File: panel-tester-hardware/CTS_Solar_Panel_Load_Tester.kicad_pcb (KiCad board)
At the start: 2 copper layers, 57 x 67.5 mm, 18 parts, among them J1 Screw_Terminal_01x02, J2 Conn_01x02_Pin, J3 Conn_01x07, J4 Conn_01x03, U1 INA219AxD, U2 YAAJ_BluePill

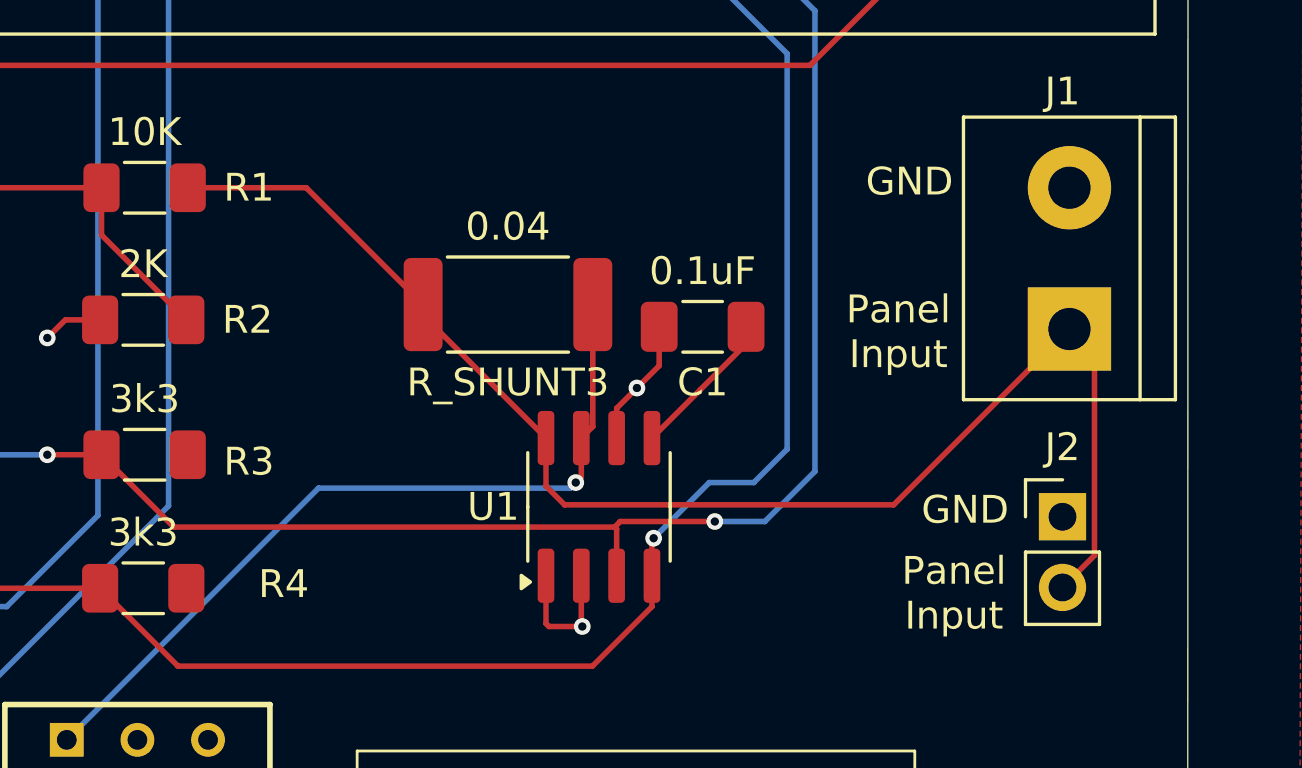
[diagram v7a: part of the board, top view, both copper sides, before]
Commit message: Add 1 mm net class for high current path
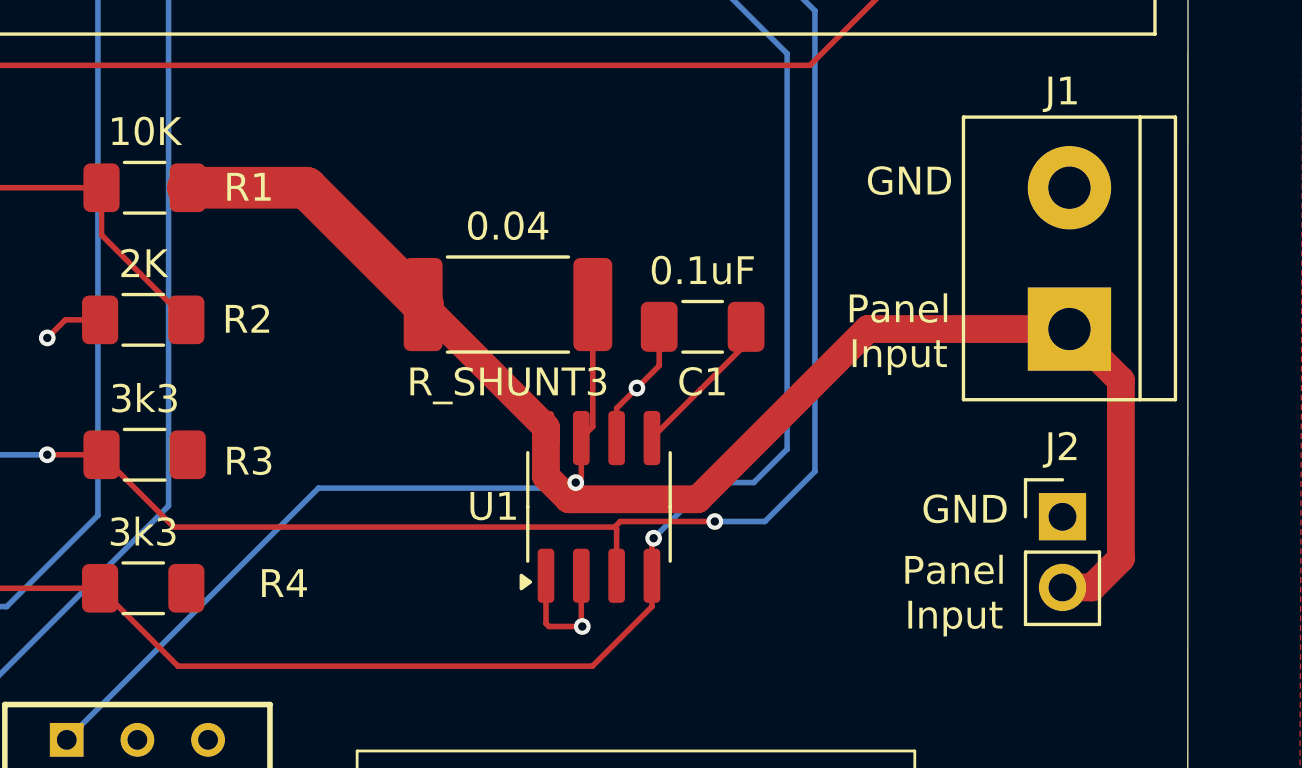
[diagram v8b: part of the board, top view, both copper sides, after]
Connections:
- RV1 pad 1: Net-(U1-IN-) -> V_SOLAR_INPUT_POS
- R_SHUNT3 pad 2: Net-(U1-IN-) -> V_SOLAR_INPUT_POS
- U1 pad 7: Net-(U1-IN-) -> V_SOLAR_INPUT_POS
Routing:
- net V_SOLAR_INPUT_POS: track 50.4 -> 80.2 mm, vias 0 -> 1
- net Net-(U1-IN-): track 28.8 -> 0.00 mm, vias 1 -> 0
